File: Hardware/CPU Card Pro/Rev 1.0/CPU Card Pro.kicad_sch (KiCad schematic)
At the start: 17 parts, among them J1 6502 Card Edge, J2 BANK ADDR, J3 EXP, U1 65C816, U2 74HC00, U3 74HC245, U4 74HC573

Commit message: Add BOMs
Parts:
- J2: now in the parts list
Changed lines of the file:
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@@
+			)
+		)
+		(property "Note" ""
+			(at 50.8 58.42 0)
+			(hide yes)
+			(show_name no)
+			(do_not_autoplace no)
+			(effects
+				(font
+					(size 1.27 1.27)
+				)
 			)
 		)
@@
 			)
 		)
+		(property "Note" ""
+			(at 100.33 35.56 0)
+			(hide yes)
+			(show_name no)
+			(do_not_autoplace no)
+			(effects
+				(font
+					(size 1.27 1.27)
+				)
+			)
+		)
 		(pin "10"
 		)
@@
 			)
 		)
+		(property "Note" ""
+			(at 208.28 38.1 90)
+			(hide yes)
+			(show_name no)
+			(do_not_autoplace no)
+			(effects
+				(font
+					(size 1.27 1.27)
+				)
+			)
+		)
 		(pin "2"
 		)
@@
 			)
 		)
+		(property "Note" ""
+			(at 208.28 45.72 90)
+			(hide yes)
+			(show_name no)
+			(do_not_autoplace no)
+			(effects
+				(font
+					(size 1.27 1.27)
+				)
+			)
+		)
 		(pin "1"
 		)
@@
 			)
 		)
+		(property "Note" ""
+			(at 208.28 53.34 90)
+			(hide yes)
+			(show_name no)
+			(do_not_autoplace no)
+			(effects
+				(font
+					(size 1.27 1.27)
+				)
+			)
+		)
 		(pin "1"
 		)
@@
 			)
 		)
+		(property "Note" ""
+			(at 208.28 60.96 90)
+			(hide yes)
+			(show_name no)
+			(do_not_autoplace no)
+			(effects
+				(font
+					(size 1.27 1.27)
+				)
+			)
+		)
 		(pin "1"
 		)
@@
 			)
 		)
+		(property "Note" ""
+			(at 208.28 68.58 90)
+			(hide yes)
+			(show_name no)
+			(do_not_autoplace no)
+			(effects
+				(font
+					(size 1.27 1.27)
+				)
+			)
+		)
 		(pin "2"
 		)
@@
 		)
 		(property "LCSC" "C49678"
+			(at 198.12 86.36 0)
+			(hide yes)
+			(show_name no)
+			(do_not_autoplace no)
+			(effects
+				(font
+					(size 1.27 1.27)
+				)
+			)
+		)
+		(property "Note" ""
 			(at 198.12 86.36 0)
 			(hide yes)
@@
 			)
 		)
+		(property "Note" ""
+			(at 115.57 123.19 0)
+			(hide yes)
+			(show_name no)
+			(do_not_autoplace no)
+			(effects
+				(font
+					(size 1.27 1.27)
+				)
+			)
+		)
 		(pin "2"
 		)
@@
 			)
 		)
+		(property "Note" ""
+			(at 241.3 119.38 0)
+			(hide yes)
+			(show_name no)
+			(do_not_autoplace no)
+			(effects
+				(font
+					(size 1.27 1.27)
+				)
+			)
+		)
 		(pin "1"
 		)
@@
 			)
 		)
+		(property "Note" ""
+			(at 218.44 119.38 0)
+			(hide yes)
+			(show_name no)
+			(do_not_autoplace no)
+			(effects
+				(font
+					(size 1.27 1.27)
+				)
+			)
+		)
 		(pin "1"
 		)
@@
 		)
 		(property "Description" "Generic connector, double row, 02x04, odd/even pin numbering scheme (row 1 odd numbers, row 2 even numbers), script generated (kicad-library-utils/schlib/autogen/connector/)"
+			(at 114.3 170.18 0)
+			(hide yes)
+			(show_name no)
+			(do_not_autoplace no)
+			(effects
+				(font
+					(size 1.27 1.27)
+				)
+			)
+		)
+		(property "Note" ""
 			(at 114.3 170.18 0)
 			(hide yes)
@@
 			)
 		)
+		(property "Note" ""
+			(at 170.18 149.86 0)
+			(hide yes)
+			(show_name no)
+			(do_not_autoplace no)
+			(effects
+				(font
+					(size 1.27 1.27)
+				)
+			)
+		)
 		(pin "1"
 		)
@@
 			)
 		)
+		(property "Note" ""
+			(at 157.48 149.86 0)
+			(hide yes)
+			(show_name no)
+			(do_not_autoplace no)
+			(effects
+				(font
+					(size 1.27 1.27)
+				)
+			)
+		)
 		(pin "1"
 		)
@@
 		(property "LCSC" "C17513"
 			(at 208.28 76.2 0)
+			(hide yes)
+			(show_name no)
+			(do_not_autoplace no)
+			(effects
+				(font
+					(size 1.27 1.27)
+				)
+			)
+		)
+		(property "Note" ""
+			(at 208.28 76.2 90)
 			(hide yes)
 			(show_name no)
@@
 			)
 		)
+		(property "Note" ""
+			(at 229.87 149.86 0)
+			(hide yes)
+			(show_name no)
+			(do_not_autoplace no)
+			(effects
+				(font
+					(size 1.27 1.27)
+				)
+			)
+		)
 		(pin "1"
 		)
@@
 		(body_style 1)
 		(exclude_from_sim no)
-		(in_bom no)
+		(in_bom yes)
 		(on_board yes)
 		(in_pos_files yes)
@@
 		)
 		(property "Description" "Generic connector, double row, 02x05, odd/even pin numbering scheme (row 1 odd numbers, row 2 even numbers), script generated (kicad-library-utils/schlib/autogen/connector/)"
+			(at 166.37 119.38 0)
+			(hide yes)
+			(show_name no)
+			(do_not_autoplace no)
+			(effects
+				(font
+					(size 1.27 1.27)
+				)
+			)
+		)
+		(property "Note" ""
 			(at 166.37 119.38 0)
 			(hide yes)
@@
 			)
 		)
+		(property "Note" ""
+			(at 71.12 171.45 0)
+			(hide yes)
+			(show_name no)
+			(do_not_autoplace no)
+			(effects
+				(font
+					(size 1.27 1.27)
+				)
+			)
+		)
 		(pin "1"
 		)
@@
 		)
 		(property "LCSC" "C49678"
+			(at 182.88 149.86 0)
+			(hide yes)
+			(show_name no)
+			(do_not_autoplace no)
+			(effects
+				(font
+					(size 1.27 1.27)
+				)
+			)
+		)
+		(property "Note" ""
 			(at 182.88 149.86 0)
 			(hide yes)
@@
 			)
 		)
+		(property "Note" ""
+			(at 198.12 149.86 0)
+			(hide yes)
+			(show_name no)
+			(do_not_autoplace no)
+			(effects
+				(font
+					(size 1.27 1.27)
+				)
+			)
+		)
 		(pin "1"
 		)
@@
 			(at 50.8 123.19 0)
 			(hide yes)
+			(show_name no)
+			(do_not_autoplace no)
+			(effects
+				(font
+					(size 1.27 1.27)
+				)
+			)
+		)
+		(property "Note" ""
+			(at 50.8 123.19 0)
+			(hide yes)

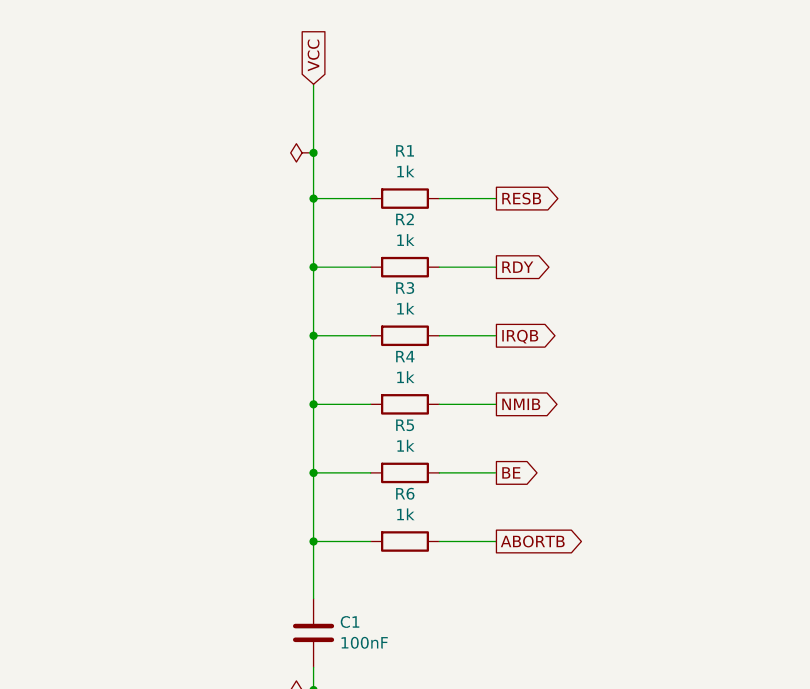
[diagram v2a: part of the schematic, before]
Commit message: Change pull up resistor values
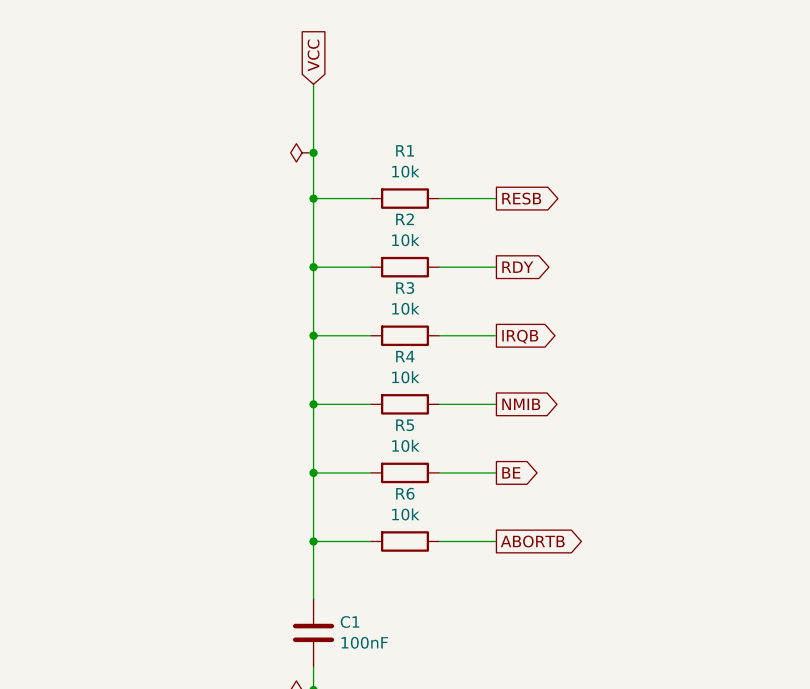
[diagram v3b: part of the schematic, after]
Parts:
- R1, R2, R3, R4, R5, R6: value 1k -> 10k; LCSC C17513 -> C2930231
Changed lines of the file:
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@@
 			)
 		)
-		(property "Value" "1k"
+		(property "Value" "10k"
 			(at 208.28 35.1536 90)
 			(show_name no)
@@
 			)
 		)
-		(property "LCSC" "C17513"
+		(property "LCSC" "C2930231"
 			(at 208.28 38.1 0)
 			(hide yes)
@@
 			)
 		)
-		(property "Value" "1k"
+		(property "Value" "10k"
 			(at 208.28 42.7736 90)
 			(show_name no)
@@
 			)
 		)
-		(property "LCSC" "C17513"
+		(property "LCSC" "C2930231"
 			(at 208.28 45.72 0)
 			(hide yes)
@@
 			)
 		)
-		(property "Value" "1k"
+		(property "Value" "10k"
 			(at 208.28 50.3936 90)
 			(show_name no)
@@
 			)
 		)
-		(property "LCSC" "C17513"
+		(property "LCSC" "C2930231"
 			(at 208.28 53.34 0)
 			(hide yes)
@@
 			)
 		)
-		(property "Value" "1k"
+		(property "Value" "10k"
 			(at 208.28 58.0136 90)
 			(show_name no)
@@
 			)
 		)
-		(property "LCSC" "C17513"
+		(property "LCSC" "C2930231"
 			(at 208.28 60.96 0)
 			(hide yes)
@@
 			)
 		)
-		(property "Value" "1k"
+		(property "Value" "10k"
 			(at 208.28 65.6336 90)
 			(show_name no)
@@
 			)
 		)
-		(property "LCSC" "C17513"
+		(property "LCSC" "C2930231"
 			(at 208.28 68.58 0)
 			(hide yes)
@@
 			)
 		)
-		(property "Value" "1k"
+		(property "Value" "10k"
 			(at 208.28 73.2536 90)
 			(show_name no)
@@
 			)
 		)
-		(property "LCSC" "C17513"
+		(property "LCSC" "C2930231"
 			(at 208.28 76.2 0)
 			(hide yes)

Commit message: Add BOMs to README
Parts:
- J2, J3, U1: now left out of the parts list
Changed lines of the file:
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@@
 		(body_style 1)
 		(exclude_from_sim no)
-		(in_bom yes)
+		(in_bom no)
 		(on_board yes)
 		(in_pos_files yes)
@@
 		(body_style 1)
 		(exclude_from_sim no)
-		(in_bom yes)
+		(in_bom no)
 		(on_board yes)
 		(in_pos_files yes)
@@
 		(body_style 1)
 		(exclude_from_sim no)
-		(in_bom yes)
-		(on_board yes)
-		(in_pos_files yes)
+		(in_bom no)
+		(on_board yes)
+		(in_pos_files yes)
